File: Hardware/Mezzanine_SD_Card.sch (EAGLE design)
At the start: 8 parts, among them U2 EDISON_CONNECTOR_FULLMOUNTING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, U3 EDISON_CONNECTOR_FULLHEADER

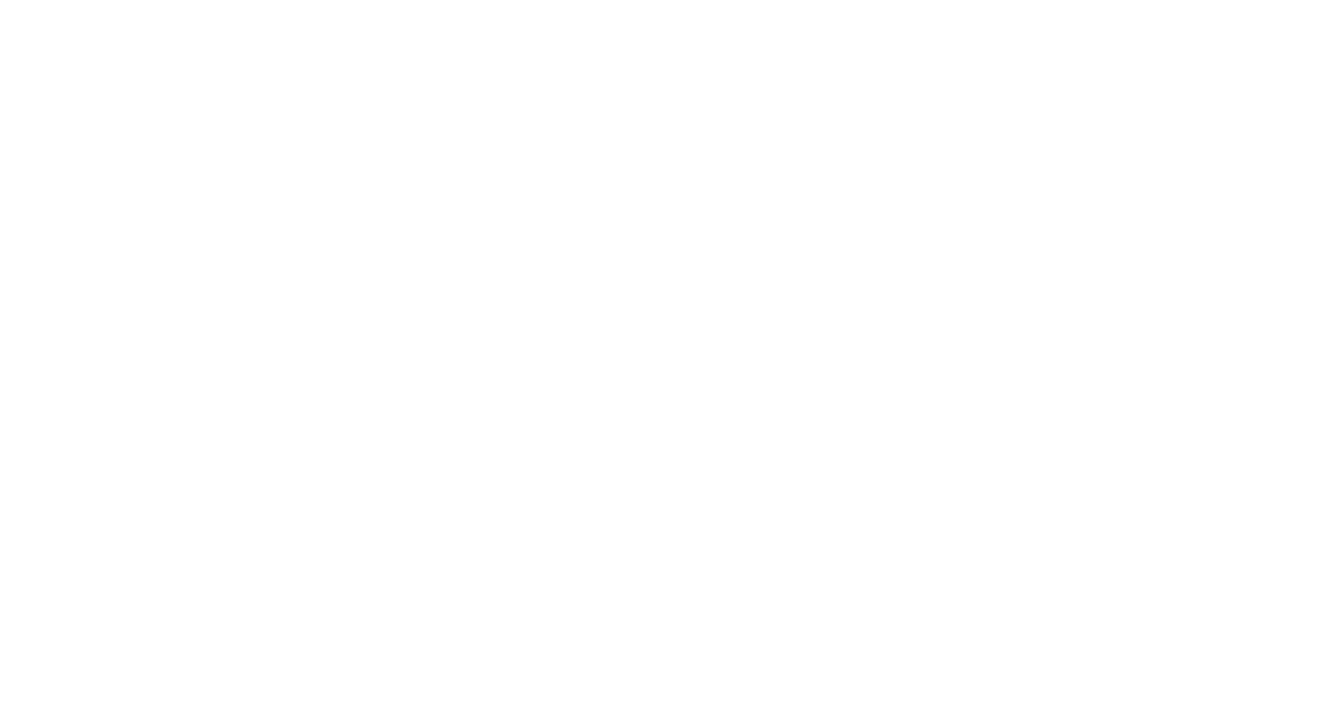
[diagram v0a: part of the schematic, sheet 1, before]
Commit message: renamed template and added SD, still needs work for level shifting
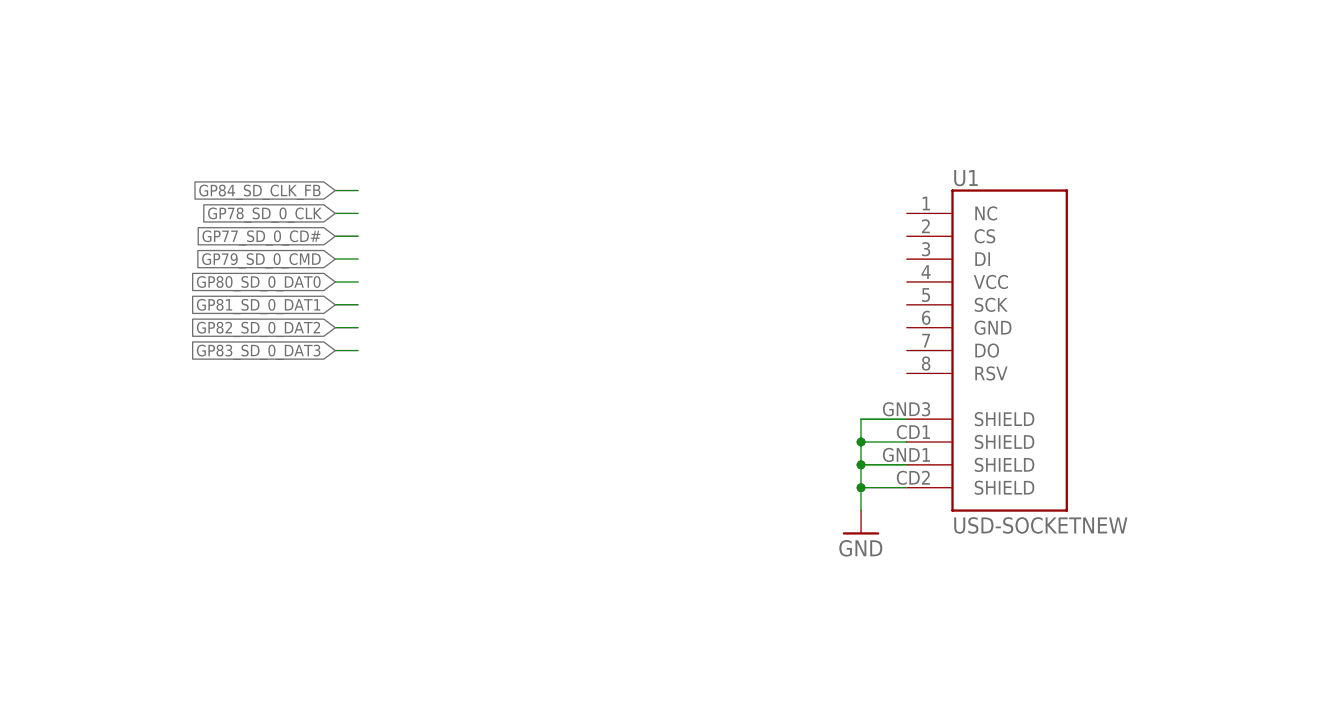
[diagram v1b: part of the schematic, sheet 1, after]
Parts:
- added U1: USD-SOCKETNEW, SparkFun-Connectors:USD-SOCKETNEW
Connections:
- net GND: now also U1.SHIELD@1, U1.SHIELD@2, U1.SHIELD@3, U1.SHIELD@4
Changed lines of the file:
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@@
 <part name="FID1" library="SparkFun-Aesthetics" deviceset="FIDUCIAL" device="1X2"/>
 <part name="FID2" library="SparkFun-Aesthetics" deviceset="FIDUCIAL" device="1X2"/>
+<part name="U1" library="SparkFun-Connectors" deviceset="USD-SOCKET" device="NEW"/>
+<part name="GND1" library="SparkFun-Aesthetics" deviceset="GND" device=""/>
 </parts>
 <sheets>
@@
 <instance part="FID1" gate="G$1" x="246.38" y="25.4"/>
 <instance part="FID2" gate="G$1" x="241.3" y="25.4"/>
+<instance part="U1" gate="G$1" x="160.02" y="111.76"/>
+<instance part="GND1" gate="1" x="147.32" y="88.9"/>
 </instances>
 <busses>
 </busses>
 <nets>
+<net name="GND" class="0">
+<segment>
+<pinref part="U1" gate="G$1" pin="SHIELD@1"/>
+<wire x1="152.4" y1="101.6" x2="147.32" y2="101.6" width="0.1524" layer="91"/>
+<wire x1="147.32" y1="101.6" x2="147.32" y2="99.06" width="0.1524" layer="91"/>
+<pinref part="U1" gate="G$1" pin="SHIELD@4"/>
+<wire x1="147.32" y1="99.06" x2="147.32" y2="96.52" width="0.1524" layer="91"/>
+<wire x1="147.32" y1="96.52" x2="147.32" y2="93.98" width="0.1524" layer="91"/>
+<wire x1="147.32" y1="93.98" x2="152.4" y2="93.98" width="0.1524" layer="91"/>
+<pinref part="U1" gate="G$1" pin="SHIELD@3"/>
+<wire x1="152.4" y1="96.52" x2="147.32" y2="96.52" width="0.1524" layer="91"/>
+<pinref part="U1" gate="G$1" pin="SHIELD@2"/>
+<wire x1="147.32" y1="99.06" x2="152.4" y2="99.06" width="0.1524" layer="91"/>
+<junction x="147.32" y="96.52"/>
+<junction x="147.32" y="99.06"/>
+<pinref part="GND1" gate="1" pin="GND"/>
+<wire x1="147.32" y1="91.44" x2="147.32" y2="93.98" width="0.1524" layer="91"/>
+<junction x="147.32" y="93.98"/>
+</segment>
+</net>
+<net name="GP84_SD_CLK_FB" class="0">
+<segment>
+<wire x1="91.44" y1="127" x2="88.9" y2="127" width="0.1524" layer="91"/>
+<label x="88.9" y="127" size="1.27" layer="95" rot="R180" xref="yes"/>
+</segment>
+</net>
+<net name="GP78_SD_0_CLK" class="0">
+<segment>
+<wire x1="91.44" y1="124.46" x2="88.9" y2="124.46" width="0.1524" layer="91"/>
+<label x="88.9" y="124.46" size="1.27" layer="95" rot="R180" xref="yes"/>
+</segment>
+</net>
+<net name="GP77_SD_0_CD#" class="0">
+<segment>
+<wire x1="91.44" y1="121.92" x2="88.9" y2="121.92" width="0.1524" layer="91"/>
+<label x="88.9" y="121.92" size="1.27" layer="95" rot="R180" xref="yes"/>
+</segment>
+</net>
+<net name="GP79_SD_0_CMD" class="0">
+<segment>
+<wire x1="91.44" y1="119.38" x2="88.9" y2="119.38" width="0.1524" layer="91"/>
+<label x="88.9" y="119.38" size="1.27" layer="95" rot="R180" xref="yes"/>
+</segment>
+</net>
+<net name="GP80_SD_0_DAT0" class="0">
+<segment>
+<wire x1="91.44" y1="116.84" x2="88.9" y2="116.84" width="0.1524" layer="91"/>
+<label x="88.9" y="116.84" size="1.27" layer="95" rot="R180" xref="yes"/>
+</segment>
+</net>
+<net name="GP81_SD_0_DAT1" class="0">
+<segment>
+<wire x1="91.44" y1="114.3" x2="88.9" y2="114.3" width="0.1524" layer="91"/>
+<label x="88.9" y="114.3" size="1.27" layer="95" rot="R180" xref="yes"/>
+</segment>
+</net>
+<net name="GP82_SD_0_DAT2" class="0">
+<segment>
+<wire x1="91.44" y1="111.76" x2="88.9" y2="111.76" width="0.1524" layer="91"/>
+<label x="88.9" y="111.76" size="1.27" layer="95" rot="R180" xref="yes"/>
+</segment>
+</net>
+<net name="GP83_SD_0_DAT3" class="0">
+<segment>
+<wire x1="91.44" y1="109.22" x2="88.9" y2="109.22" width="0.1524" layer="91"/>
+<label x="88.9" y="109.22" size="1.27" layer="95" rot="R180" xref="yes"/>
+</segment>
+</net>
 </nets>
 </sheet>
